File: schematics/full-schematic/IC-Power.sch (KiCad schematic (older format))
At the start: 2 parts, among them U2 74LS04, U4 74LS32

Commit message: Schematics
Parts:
- U4: footprint (none) -> Package_SO:SOIC-14_3.9x8.7mm_P1.27mm
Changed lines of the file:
@@
 EESchema Schematic File Version 4
-LIBS:full-schematic-cache
-EELAYER 29 0
+EELAYER 30 0
 EELAYER END
 $Descr A4 11693 8268
 encoding utf-8
-Sheet 3 3
+Sheet 3 4
 Title ""
 Date ""
@@
 F 0 "U4" H 2800 2150 50  0000 C CNN
 F 1 "74LS32" H 3200 2150 50  0000 C CNN
-F 2 "" H 3000 1800 50  0001 C CNN
+F 2 "Package_SO:SOIC-14_3.9x8.7mm_P1.27mm" H 3000 1800 50  0001 C CNN
 F 3 "http://www.ti.com/lit/gpn/sn74LS32" H 3000 1800 50  0001 C CNN
 	5    3000 1800

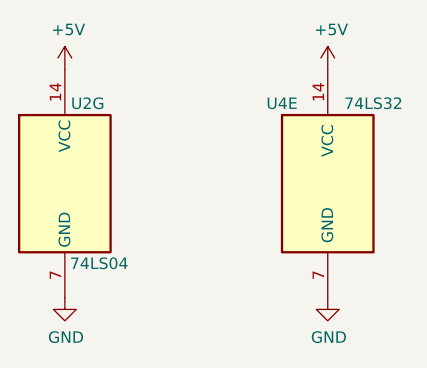
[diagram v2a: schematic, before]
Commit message: Schematic updates
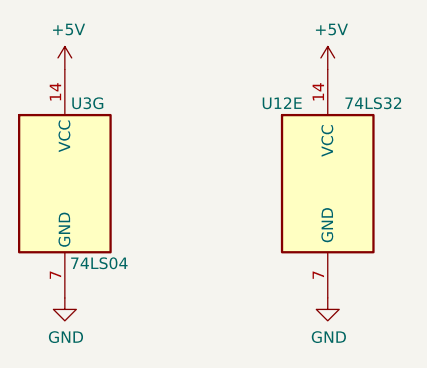
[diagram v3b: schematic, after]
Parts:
- renumbered U4 to U12, U2 to U3
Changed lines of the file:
@@
 EESchema Schematic File Version 4
-LIBS:full-schematic-cache
 EELAYER 30 0
 EELAYER END
 $Descr A4 11693 8268
 encoding utf-8
-Sheet 3 4
+Sheet 3 5
 Title ""
 Date ""
@@
 P 1850 1800
 AR Path="/5DEB49FB" Ref="U?"  Part="7"
-AR Path="/5DEAD379/5DEB49FB" Ref="U2"  Part="7"
-F 0 "U2" H 1950 2150 50  0000 C CNN
+AR Path="/5DEAD379/5DEB49FB" Ref="U3"  Part="7"
+F 0 "U3" H 1950 2150 50  0000 C CNN
 F 1 "74LS04" H 2000 1450 50  0000 C CNN
 F 2 "Package_SO:SOIC-14_3.9x8.7mm_P1.27mm" H 1850 1800 50  0001 C CNN
@@
 P 1850 1300
 AR Path="/5DEB4A01" Ref="#PWR?"  Part="1"
-AR Path="/5DEAD379/5DEB4A01" Ref="#PWR024"  Part="1"
-F 0 "#PWR024" H 1850 1150 50  0001 C CNN
+AR Path="/5DEAD379/5DEB4A01" Ref="#PWR025"  Part="1"
+F 0 "#PWR025" H 1850 1150 50  0001 C CNN
 F 1 "+5V" H 1865 1473 50  0000 C CNN
 F 2 "" H 1850 1300 50  0001 C CNN
@@
 P 1850 2300
 AR Path="/5DEB4A07" Ref="#PWR?"  Part="1"
-AR Path="/5DEAD379/5DEB4A07" Ref="#PWR025"  Part="1"
-F 0 "#PWR025" H 1850 2050 50  0001 C CNN
+AR Path="/5DEAD379/5DEB4A07" Ref="#PWR026"  Part="1"
+F 0 "#PWR026" H 1850 2050 50  0001 C CNN
 F 1 "GND" H 1855 2127 50  0000 C CNN
 F 2 "" H 1850 2300 50  0001 C CNN
@@
 P 3000 1800
 AR Path="/5D5CBDC9/5DECAA88" Ref="U?"  Part="5"
-AR Path="/5DEAD379/5DECAA88" Ref="U4"  Part="5"
-F 0 "U4" H 2800 2150 50  0000 C CNN
+AR Path="/5DEAD379/5DECAA88" Ref="U12"  Part="5"
+F 0 "U12" H 2800 2150 50  0000 C CNN
 F 1 "74LS32" H 3200 2150 50  0000 C CNN
 F 2 "Package_SO:SOIC-14_3.9x8.7mm_P1.27mm" H 3000 1800 50  0001 C CNN
@@
 AR Path="/5DECAA8E" Ref="#PWR?"  Part="1"
 AR Path="/5D5CBDC9/5DECAA8E" Ref="#PWR?"  Part="1"
-AR Path="/5DEAD379/5DECAA8E" Ref="#PWR026"  Part="1"
-F 0 "#PWR026" H 3000 1150 50  0001 C CNN
+AR Path="/5DEAD379/5DECAA8E" Ref="#PWR027"  Part="1"
+F 0 "#PWR027" H 3000 1150 50  0001 C CNN
 F 1 "+5V" H 3015 1473 50  0000 C CNN
 F 2 "" H 3000 1300 50  0001 C CNN
@@
 AR Path="/5DECAA94" Ref="#PWR?"  Part="1"
 AR Path="/5D5CBDC9/5DECAA94" Ref="#PWR?"  Part="1"
-AR Path="/5DEAD379/5DECAA94" Ref="#PWR027"  Part="1"
-F 0 "#PWR027" H 3000 2050 50  0001 C CNN
+AR Path="/5DEAD379/5DECAA94" Ref="#PWR028"  Part="1"
+F 0 "#PWR028" H 3000 2050 50  0001 C CNN
 F 1 "GND" H 3005 2127 50  0000 C CNN
 F 2 "" H 3000 2300 50  0001 C CNN
